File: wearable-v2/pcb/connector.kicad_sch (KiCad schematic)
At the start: 46 parts, among them J1 EXT_1, J11 PNL_1, J12 PNL_2, J13 PNL_3, J14 PNL_4, J2 EXT_2, J3 EXT_3, J4 EXT_4, J7 USB_C_Receptacle_USB2.0, U1 DT1446-04V, U10 TCR3UFxxA, U2 MCP73832-2-OT, U3 S-85S1A, U4 FT201XQ

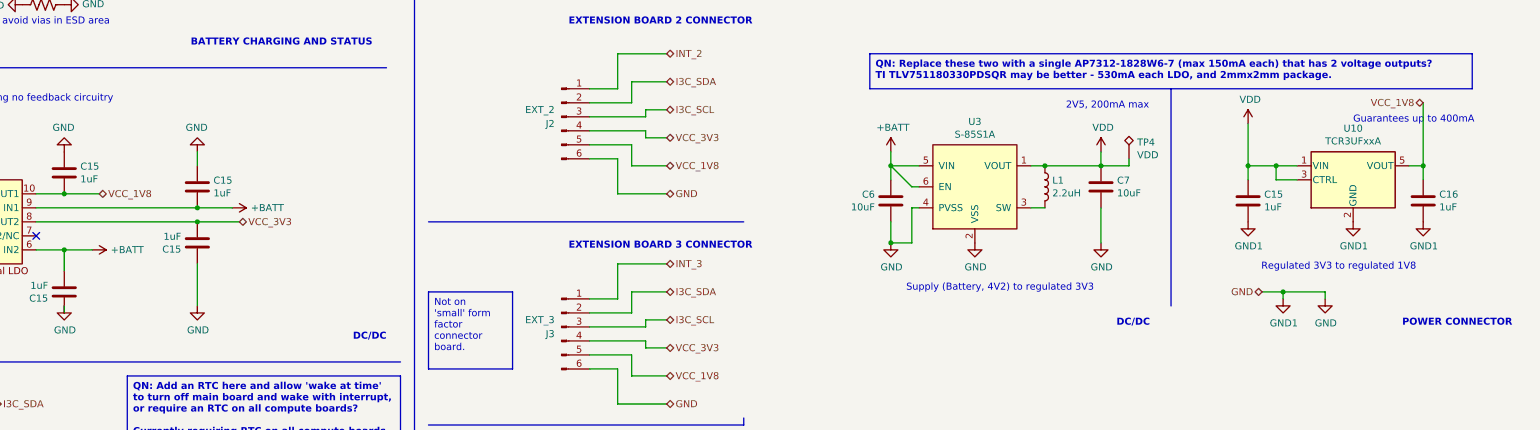
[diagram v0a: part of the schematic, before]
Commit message: Updated components and PCB layout
Signed-off-by: Adam Fowler <adam@adamfowler.org>
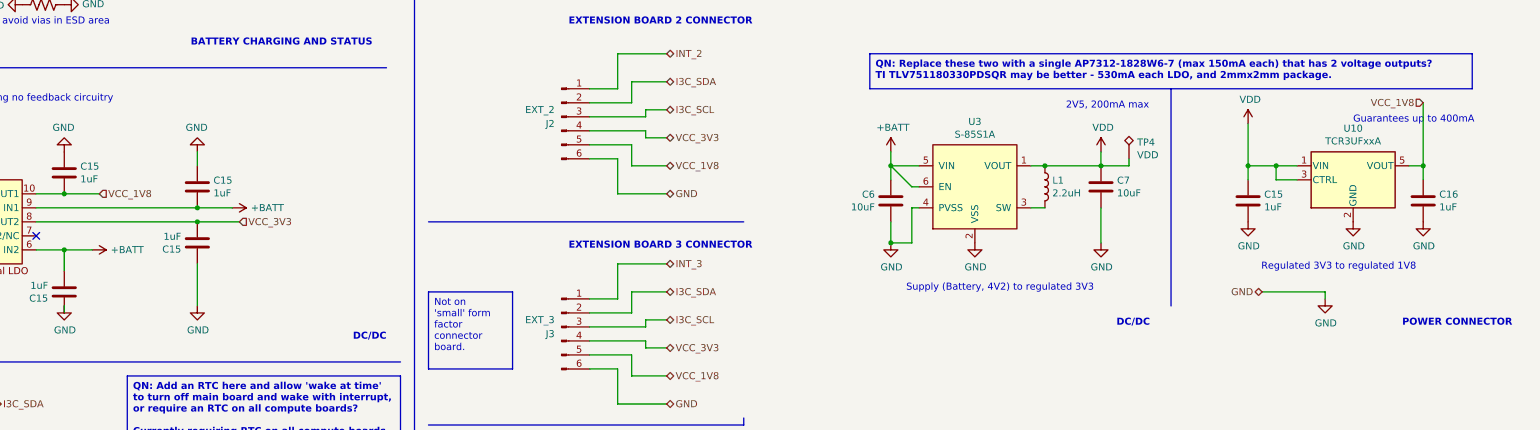
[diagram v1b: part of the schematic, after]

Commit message: Further V2 routing
Signed-off-by: Adam Fowler <adam@adamfowler.org>
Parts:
- BT1: footprint Herald_Extras:Herald_Battery_Solder_Pads -> Herald:Herald_Battery_Solder_Pads
- J7: footprint Herald_Extras:USB_C_Receptacle_IPxx -> Herald:USB_C_Receptacle_IPxx
- U1: footprint Herald_Extras:SOT-563 -> Herald:SOT-563
- U3: footprint Herald_Extras:SNT-6A -> Herald:SNT-6A
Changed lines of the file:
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@@
       (effects (font (size 1.27 1.27)))
     )
-    (property "Footprint" "Herald_Extras:SNT-6A" (at 318.77 88.9 0)
+    (property "Footprint" "Herald:SNT-6A" (at 318.77 88.9 0)
       (effects (font (size 1.27 1.27)) hide)
     )
@@
       (effects (font (size 1.27 1.27)))
     )
-    (property "Footprint" "Herald_Extras:USB_C_Receptacle_IPxx" (at 38.1 36.83 0)
+    (property "Footprint" "Herald:USB_C_Receptacle_IPxx" (at 38.1 36.83 0)
       (effects (font (size 1.27 1.27)) hide)
     )
@@
       (effects (font (size 1.27 1.27)) (justify left))
     )
-    (property "Footprint" "Herald_Extras:Herald_Battery_Solder_Pads" (at 161.29 35.306 90)
+    (property "Footprint" "Herald:Herald_Battery_Solder_Pads" (at 161.29 35.306 90)
       (effects (font (size 1.27 1.27)) hide)
     )
@@
       (effects (font (size 1.27 1.27)))
     )
-    (property "Footprint" "Herald_Extras:SOT-563" (at 69.215 54.61 0)
-      (effects (font (size 1.27 1.27)) hide)
-    )
+    (property "Footprint" "Herald:SOT-563" (at 69.215 54.61 0)
+      (effects (font (size 1.27 1.27)) hide)
+    )

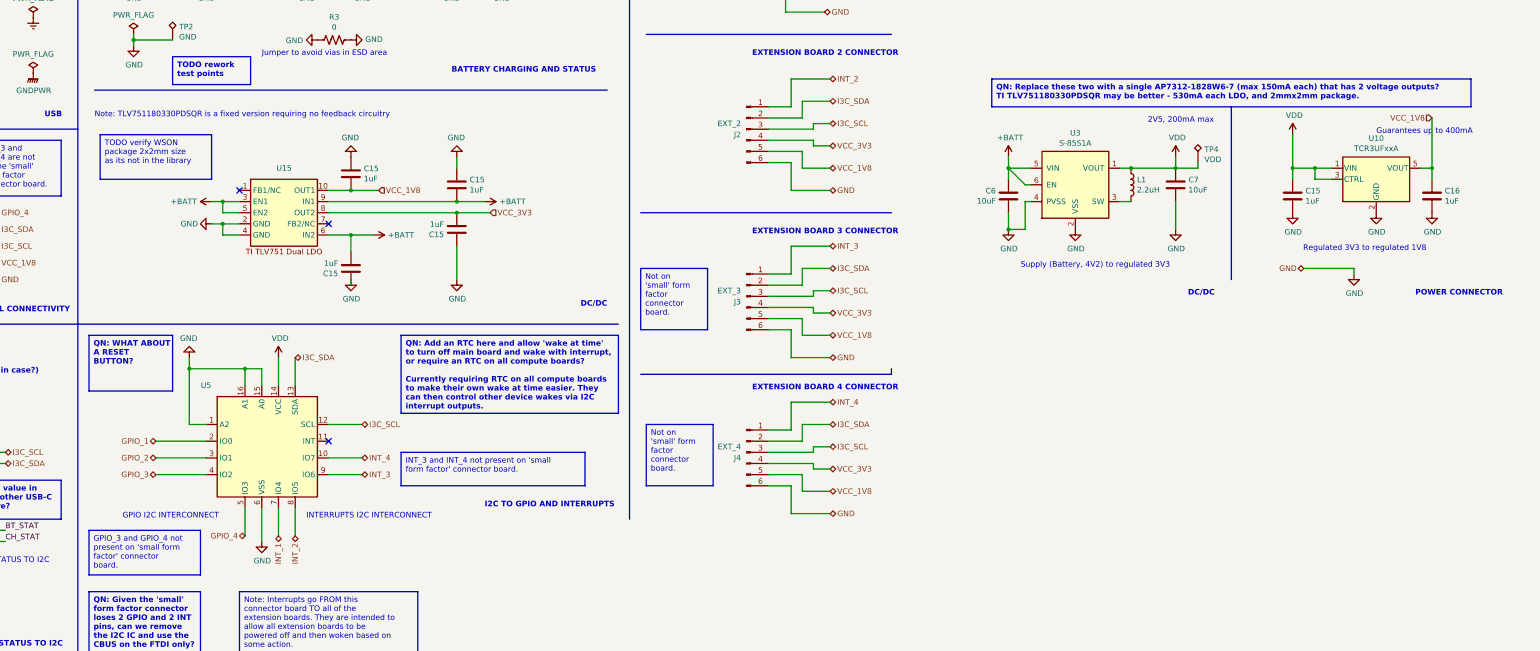
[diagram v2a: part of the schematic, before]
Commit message: Replaced unavailable I2C chip
Signed-off-by: Adam Fowler <adam@adamfowler.org>
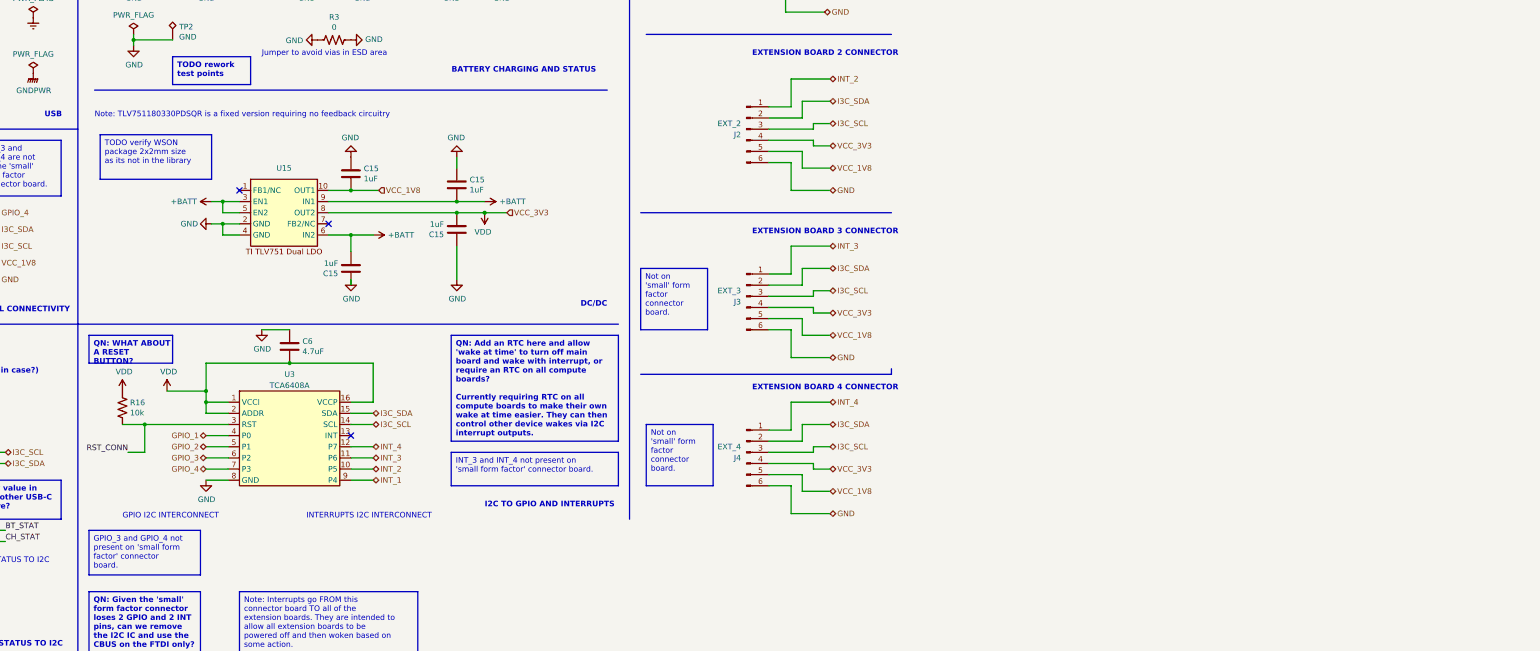
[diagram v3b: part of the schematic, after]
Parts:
- removed C15, C16: 1uF, Capacitor_SMD:C_0402_1005Metric, symbol Device:C
- removed C7: 10uF, Capacitor_SMD:C_0402_1005Metric, symbol Device:C
- removed L1: 2.2uH, Inductor_SMD:L_0603_1608Metric, symbol Device:L
- removed TP4: VDD, TestPoint:TestPoint_Pad_D1.0mm, symbol Connector:TestPoint_Alt
- removed U10: TCR3UFxxA, Package_TO_SOT_SMD:SOT-23-5, symbol Herald_Extras:TCR3UFxxA
- removed U3: S-85S1A, Herald:SNT-6A, symbol Herald_Extras:S-85S1A
- removed U5: ~, Package_DFN_QFN:TQFN-16-1EP_3x3mm_P0.5mm_EP1.23x1.23mm_ThermalVias, symbol Herald:CAT9554HV4
- added R16: 10k, Resistor_SMD:R_0402_1005Metric, symbol Device:R_US
- added U3: TCA6408A, Herald:QFN40P180X260X55-16N, symbol Herald_Extras:TCA6408A
- C6: value 10uF -> 4.7uF; MPN GRM155R60J106ME15D -> 0402YD475MAT2A
- U15: footprint Package_SON:WSON-10-1EP_2.5x2.5mm_P0.5mm_EP1.2x2mm -> Herald:SON40P200X200X80-11N
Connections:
- net VCC_3V3 is gone; now on net VDD: C15.2, J1.4 (Pin_4), J2.4 (Pin_4), J3.4 (Pin_4), J4.4 (Pin_4), U15.8 (OUT2)
- net +BATT: no longer C6.1
- net GND: now also U3.8 (GND)
- net GPIO_1: now also U3.4 (P0)
- net GPIO_2: now also U3.5 (P1)
- net GPIO_3: now also U3.6 (P2)
- net GPIO_4: now also U3.7 (P3)
- net I3C_SCL: now also U3.14 (SCL)
- net I3C_SDA: now also U3.15 (SDA)
- net INT_1: now also U3.9 (P4)
- net INT_2: now also U3.10 (P5)
- net INT_3: now also U3.11 (P6)
- net INT_4: now also U3.12 (P7)
- net VDD: now also C6.1, R16.1, U3.1 (VCCI), U3.16 (VCCP), U3.2 (ADDR)
- new net RST_CONN: R16.2, U3.3 (RST)
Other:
- note removed: "2V5, 200mA max"
- note removed: "Guarantees up to 400mA"
- note removed: "POWER CONNECTOR"
- note removed: "Regulated 3V3 to regulated 1V8"
- note removed: "Supply (Battery, 4V2) to regulated 3V3"

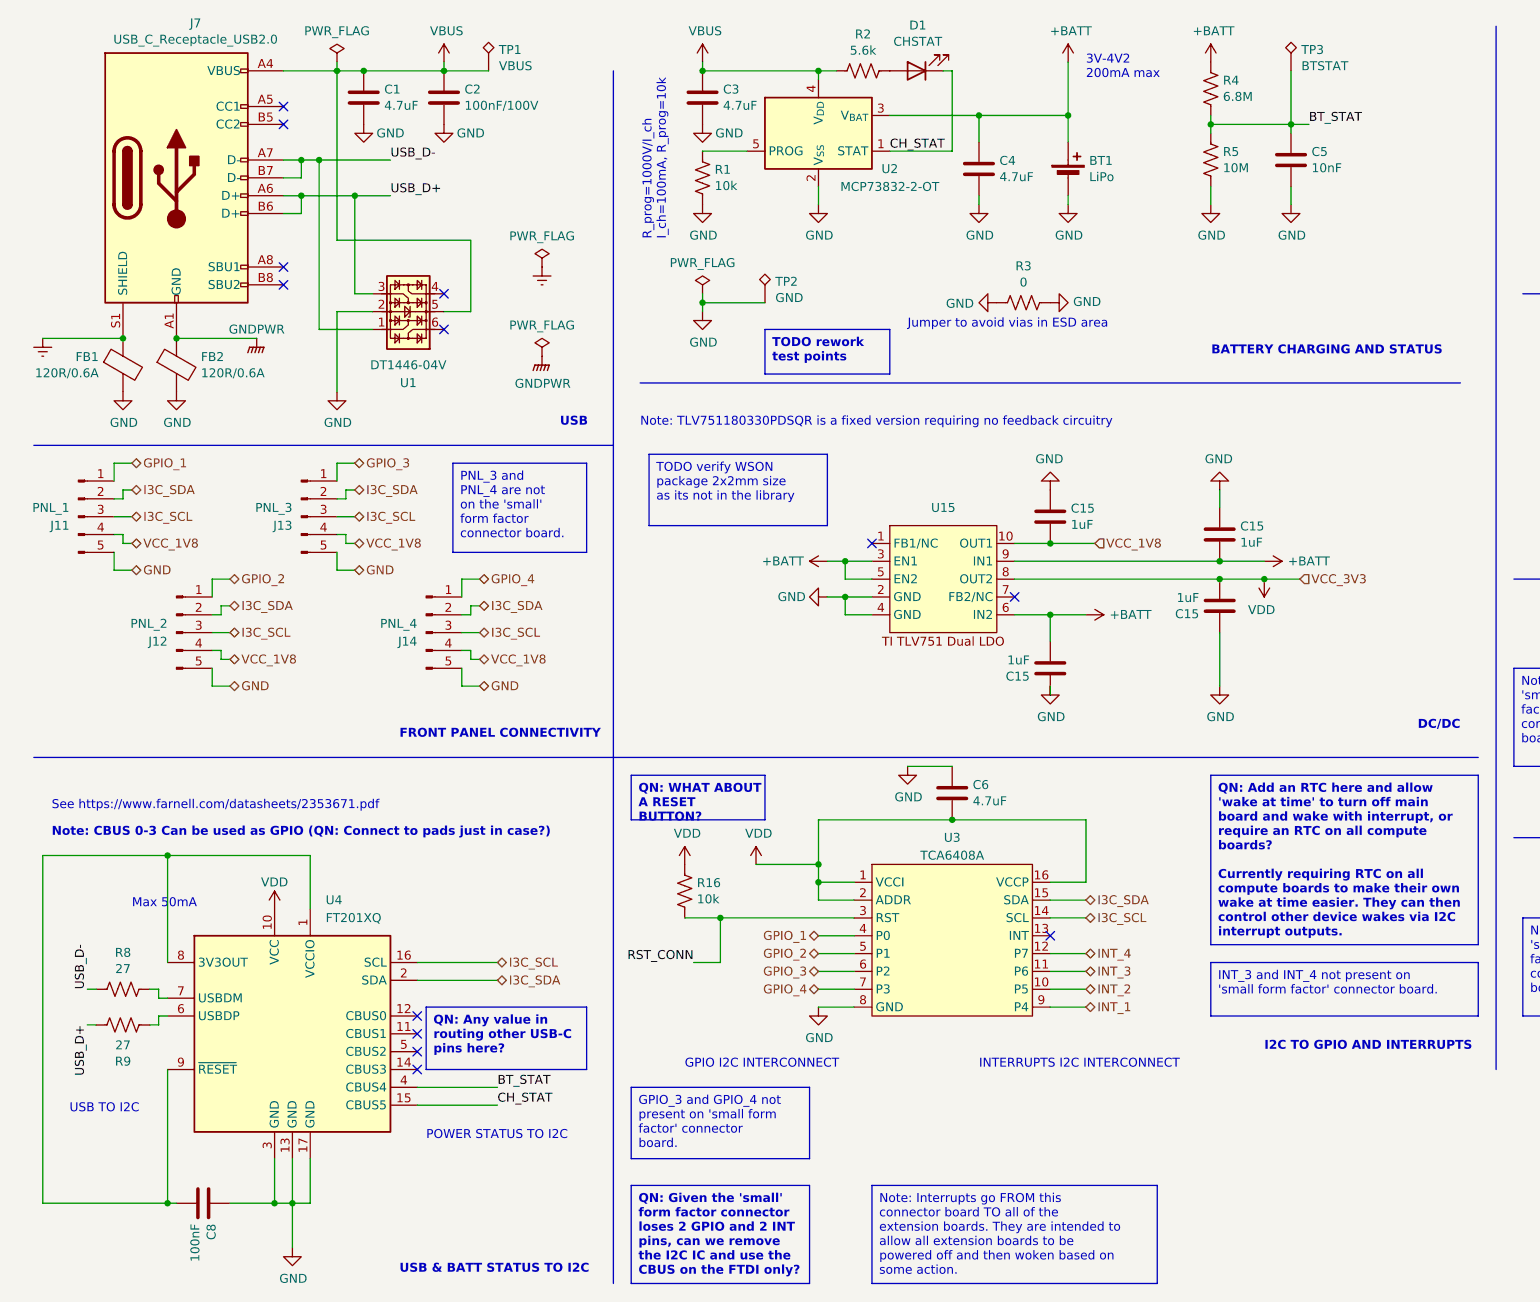
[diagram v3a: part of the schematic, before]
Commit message: Standard connector almost complete
Added JLCPCB manufacturer settings to PCB
Ensured all components are available and Tape and Reel with smallest footprint available
Signed-off-by: Adam Fowler <adam@adamfowler.org>
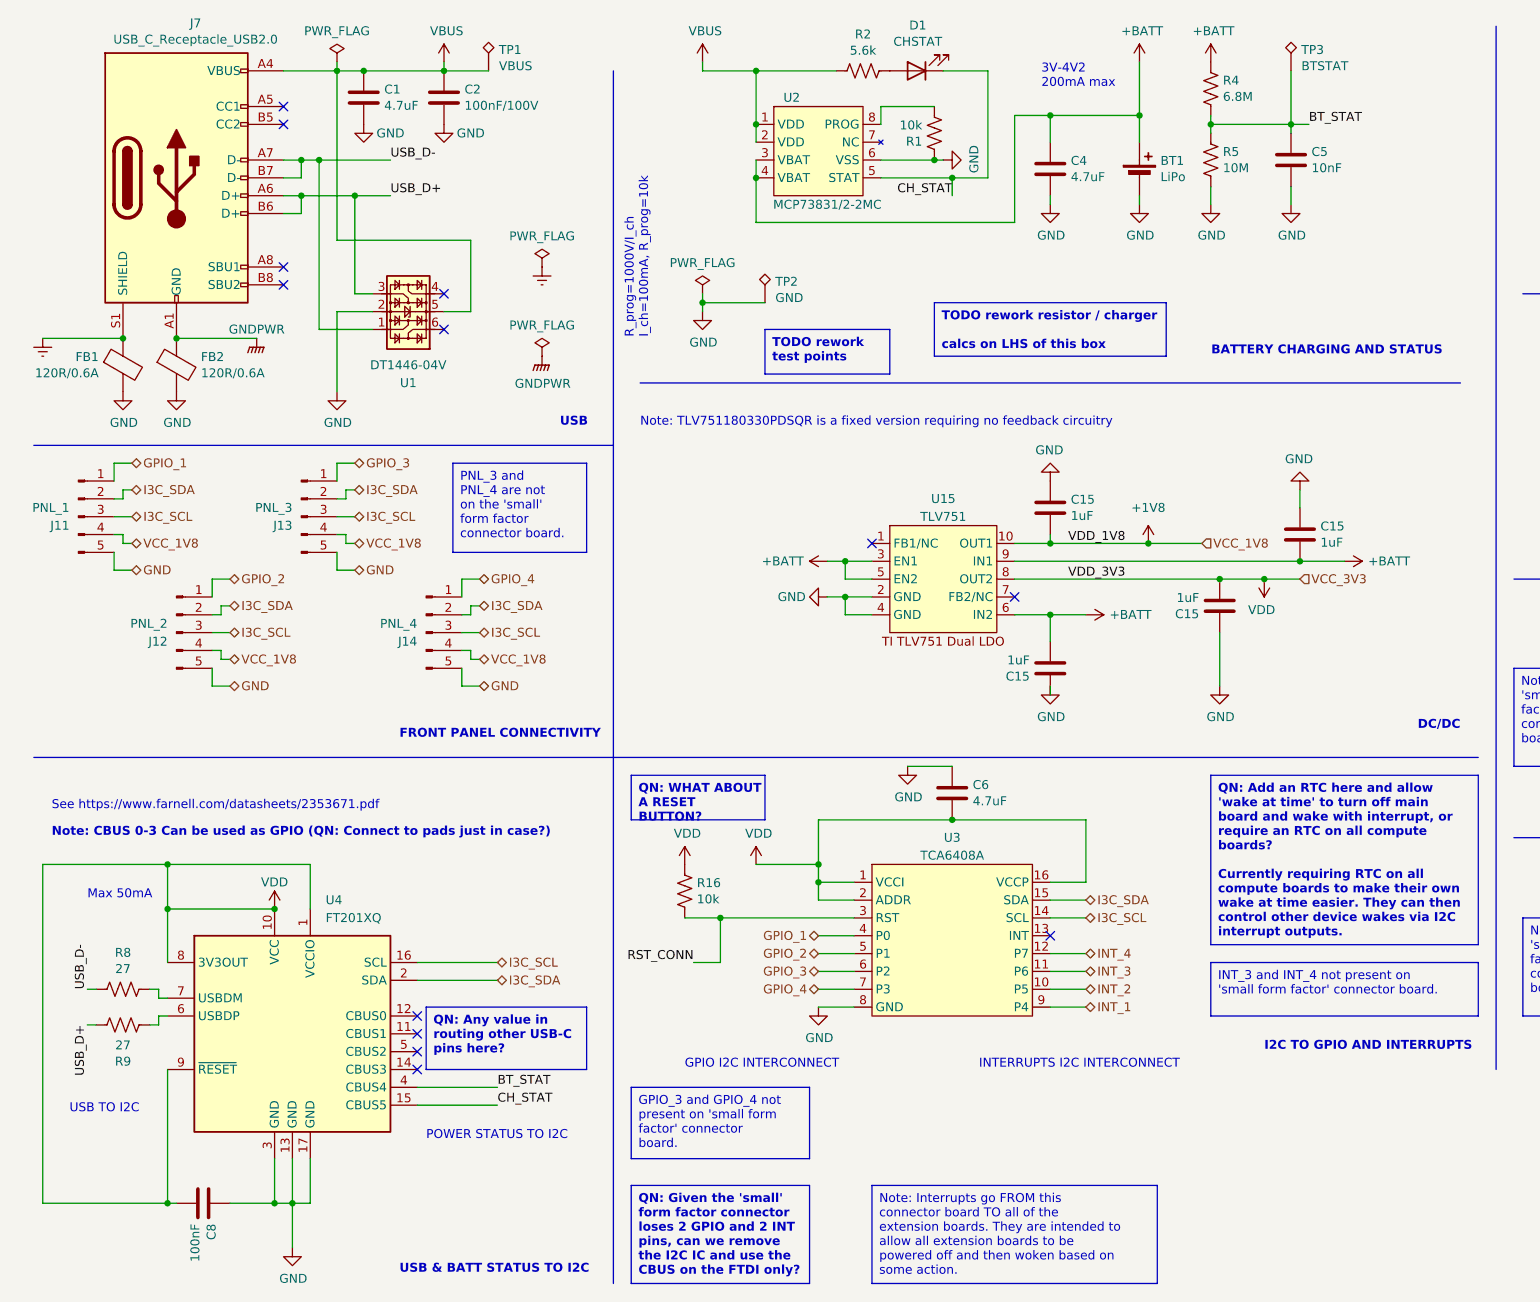
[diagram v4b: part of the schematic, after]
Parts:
- removed C3: 4.7uF, Capacitor_SMD:C_0402_1005Metric, symbol Device:C
- removed R3: 0, Resistor_SMD:R_0603_1608Metric, symbol Device:R_US
- U15: value ~ -> TLV751; MPN (none) -> TLV751180330PDSQR
- U2: value MCP73832-2-OT -> MCP73831/2-2MC; footprint Package_TO_SOT_SMD:SOT-23-5 -> Package_DFN_QFN:DFN-8-1EP_3x2mm_P0.5mm_EP1.75x1.45mm; symbol Battery_Management:MCP73832-2-OT -> Herald_Extras:MCP73831/2-2MC; MPN MCP73832T-2ACI/OT -> MCP73832T-2ACI/MC
- U3: MPN (none) -> TCA6408ARSVR
- U4: MPN (none) -> FT201XQ-R
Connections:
- net +BATT: now also U2.4 (VBAT)
- net CH_STAT: now also U2.5 (STAT); no longer U2.1 (STAT)
- net GND: now also R1.1, U2.6 (VSS); no longer R1.2, U2.2 (V_{SS})
- net VBUS: now also U2.1 (VDD), U2.2 (VDD); no longer U2.4 (V_{DD})
- net VDD: now also C8.1, U4.1 (VCCIO), U4.8 (3V3OUT), U4.9 (~{RESET})
- net VCC_1V8 renamed +1V8
- new net: R1.2, U2.8 (PROG)
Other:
- note removed: "Jumper to avoid vias in ESD area"
- moved on the sheet: BT1, C15, C4, R1
